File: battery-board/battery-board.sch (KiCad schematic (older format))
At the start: 26 parts, among them P1 CONN_01X14, P2 CONN_01X14, P3 CONN_01X02, P4 CONN_01X01, SW1 SW_PUSH, U1 BMP180, U2 MAX1724, U3 SI7021

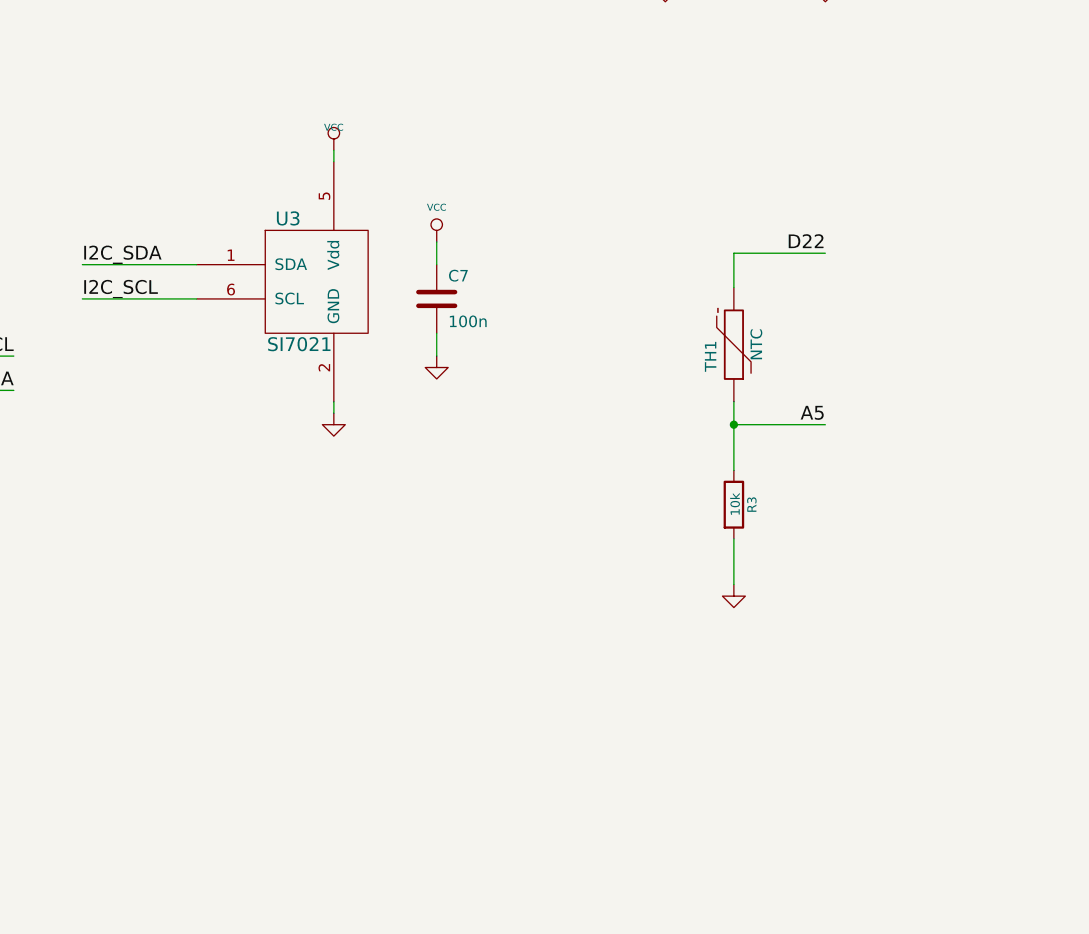
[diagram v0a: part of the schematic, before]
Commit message: New light sensor
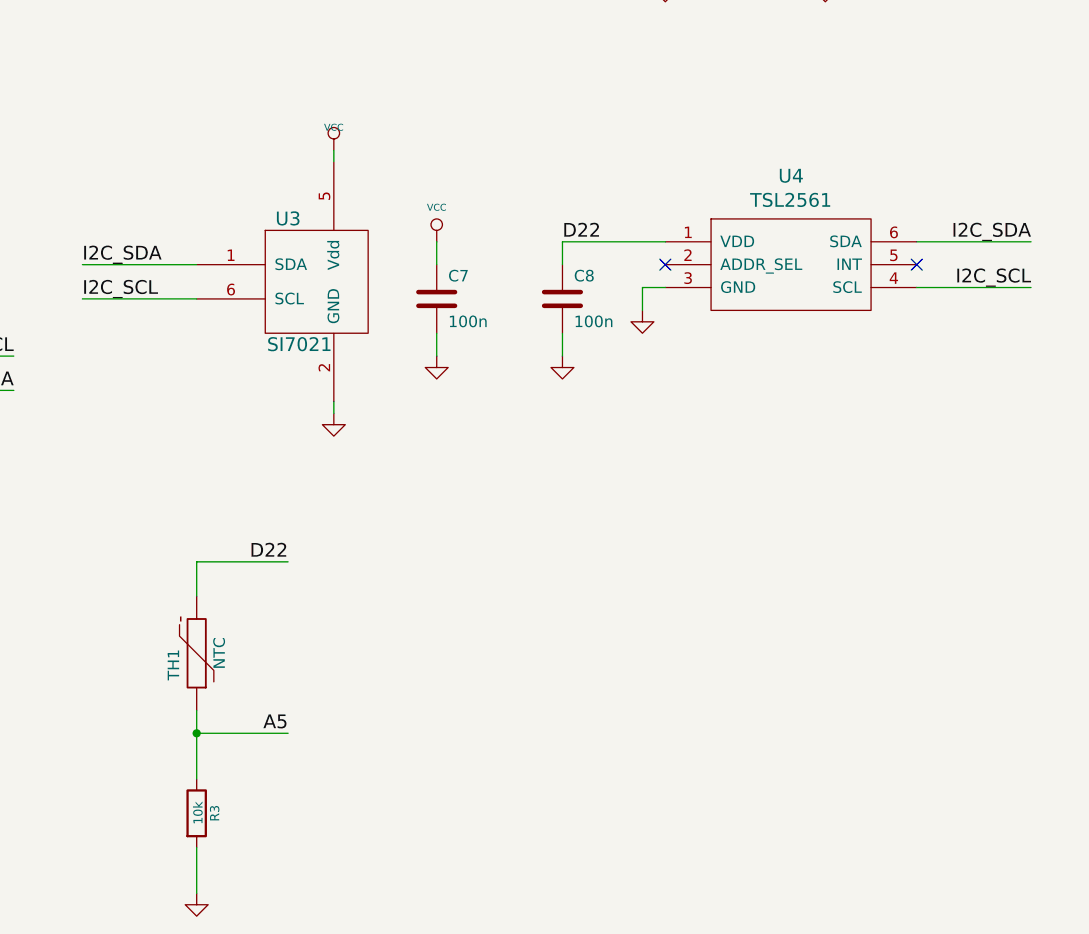
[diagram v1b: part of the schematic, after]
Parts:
- added C8: 100n, mysmd:SM0603S, symbol C
- added U4: TSL2561, mysmd:DFN-6, symbol TSL2561
- U2: footprint libcms:SOT23_6 -> libcms:SOT23-5
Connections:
- net D22: now also C8.1, U4.1 (VDD)
- net GND: now also C8.2, U4.3 (GND)
- net I2C_SCL: now also U4.4 (SCL)
- net I2C_SDA: now also U4.6 (SDA)
- no-connect marks 1 -> 3
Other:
- moved on the sheet: R3, TH1
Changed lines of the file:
@@
 EESchema Schematic File Version 2
-LIBS:battery-board-rescue
 LIBS:power
 LIBS:device
@@
 L THERMISTOR TH1
 U 1 1 5508513A
-P 8350 4450
-F 0 "TH1" V 8450 4500 50  0000 C CNN
-F 1 "NTC" V 8250 4450 50  0000 C CNN
-F 2 "mysmd:SM0603S" H 8350 4450 60  0001 C CNN
-F 3 "" H 8350 4450 60  0000 C CNN
-	1    8350 4450
+P 6000 5800
+F 0 "TH1" V 6100 5850 50  0000 C CNN
+F 1 "NTC" V 5900 5800 50  0000 C CNN
+F 2 "mysmd:SM0603S" H 6000 5800 60  0001 C CNN
+F 3 "" H 6000 5800 60  0000 C CNN
+	1    6000 5800
 	-1   0    0    1
 $EndComp
@@
 L R R3
 U 1 1 5508513B
-P 8350 5150
-F 0 "R3" V 8430 5150 40  0000 C CNN
-F 1 "10k" V 8357 5151 40  0000 C CNN
-F 2 "mysmd:SM0603S" V 8280 5150 30  0001 C CNN
-F 3 "" H 8350 5150 30  0001 C CNN
-	1    8350 5150
+P 6000 6500
+F 0 "R3" V 6080 6500 40  0000 C CNN
+F 1 "10k" V 6007 6501 40  0000 C CNN
+F 2 "mysmd:SM0603S" V 5930 6500 30  0001 C CNN
+F 3 "" H 6000 6500 30  0001 C CNN
+	1    6000 6500
 	1    0    0    -1
 $EndComp
@@
 L GND #PWR05
 U 1 1 5508513C
-P 8350 5500
-F 0 "#PWR05" H 8350 5500 30  0001 C CNN
-F 1 "GND" H 8350 5430 30  0001 C CNN
-F 2 "" H 8350 5500 60  0001 C CNN
-F 3 "" H 8350 5500 60  0001 C CNN
-	1    8350 5500
+P 6000 6850
+F 0 "#PWR05" H 6000 6850 30  0001 C CNN
+F 1 "GND" H 6000 6780 30  0001 C CNN
+F 2 "" H 6000 6850 60  0001 C CNN
+F 3 "" H 6000 6850 60  0001 C CNN
+	1    6000 6850
 	1    0    0    -1
 $EndComp
@@
 	1    0    0    -1
 $EndComp
-Text Label 8750 4800 2    60   ~ 0
+Text Label 6400 6150 2    60   ~ 0
 A5
-Text Label 8750 4050 2    60   ~ 0
+Text Label 6400 5400 2    60   ~ 0
 D22
 $Comp
@@
 F 0 "U2" H 3100 5800 60  0000 C CNN
 F 1 "MAX1724" H 2900 6400 60  0000 C CNN
-F 2 "libcms:SOT23_6" H 2950 6100 60  0001 C CNN
+F 2 "libcms:SOT23-5" H 2950 6100 60  0001 C CNN
 F 3 "" H 2950 6100 60  0000 C CNN
 	1    2950 6100
@@
 	6000 2600 6100 2600
 Wire Wire Line
-	8350 4700 8350 5000
-Wire Wire Line
-	8350 5300 8350 5500
-Wire Wire Line
-	8350 4200 8350 4050
-Wire Wire Line
-	8350 4050 8750 4050
-Wire Wire Line
-	8350 4800 8750 4800
-Connection ~ 8350 4800
+	6000 6050 6000 6350
+Wire Wire Line
+	6000 6650 6000 6850
+Wire Wire Line
+	6000 5550 6000 5400
+Wire Wire Line
+	6000 5400 6400 5400
+Wire Wire Line
+	6000 6150 6400 6150
+Connection ~ 6000 6150
 Wire Wire Line
 	3650 4300 3650 4400
@@
 	0    -1   -1   0
 $EndComp
+$Comp
+L TSL2561 U4
+U 1 1 569394C1
+P 8600 4100
+F 0 "U4" H 8600 4487 60  0000 C CNN
+F 1 "TSL2561" H 8600 4381 60  0000 C CNN
+F 2 "mysmd:DFN-6" H 8700 3850 60  0001 C CNN
+F 3 "" H 8700 3850 60  0000 C CNN
+	1    8600 4100
+	1    0    0    -1
+$EndComp
+Wire Wire Line
+	7600 4000 8050 4000
+$Comp
+L GND #PWR031
+U 1 1 56939CC4
+P 7950 4300
+F 0 "#PWR031" H 7950 4300 30  0001 C CNN
+F 1 "GND" H 7950 4230 30  0001 C CNN
+F 2 "" H 7950 4300 60  0001 C CNN
+F 3 "" H 7950 4300 60  0001 C CNN
+	1    7950 4300
+	1    0    0    -1
+$EndComp
+Wire Wire Line
+	8050 4200 7950 4200
+Wire Wire Line
+	7950 4200 7950 4300
+Text Label 9650 4200 2    60   ~ 0
+I2C_SCL
+Text Label 9650 4000 2    60   ~ 0
+I2C_SDA
+Wire Wire Line
+	9650 4000 9150 4000
+Wire Wire Line
+	9650 4200 9150 4200
+NoConn ~ 9150 4100
+NoConn ~ 8050 4100
+Text Label 7600 4000 0    60   ~ 0
+D22
+$Comp
+L C C8
+U 1 1 5693ACF1
+P 7600 4250
+F 0 "C8" H 7650 4350 50  0000 L CNN
+F 1 "100n" H 7650 4150 50  0000 L CNN
+F 2 "mysmd:SM0603S" H 7600 4250 60  0001 C CNN
+F 3 "" H 7600 4250 60  0001 C CNN
+	1    7600 4250
+	1    0    0    -1
+$EndComp
+$Comp
+L GND #PWR032
+U 1 1 5693ACF7
+P 7600 4500
+F 0 "#PWR032" H 7600 4500 30  0001 C CNN
+F 1 "GND" H 7600 4430 30  0001 C CNN
+F 2 "" H 7600 4500 60  0001 C CNN
+F 3 "" H 7600 4500 60  0001 C CNN
+	1    7600 4500
+	1    0    0    -1
+$EndComp
+Wire Wire Line
+	7600 4400 7600 4500
+Wire Wire Line
+	7600 4000 7600 4100
 $EndSCHEMATC
